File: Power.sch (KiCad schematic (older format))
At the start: 7 parts, among them J10 Conn_01x02_Female, U3 MCP73831T-2ACI_OT

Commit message: REAL COMMIT: Completed initial schematic. Added ADCs, Haptic FB circuits, test points, USB/Battery selection circuits.
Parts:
- removed D10: LED, symbol Device:LED
- added D3, D7: SS54, Diode_SMD:D_SMA_Handsoldering, symbol Device:D_Schottky
- added D4, D5, D6: 19-213/Y2C-CQ2R2L/3T, LEDs:LED_0603_HandSoldering, symbol Device:LED
- added Q1: DMG2305, Package_TO_SOT_SMD:SOT-23, symbol Transistor_FET:DMG2301L
- added R10, R11: 100k, Resistor_SMD:R_0603_1608Metric_Pad0.84x1.00mm_HandSolder, symbol Device:R
- added R8: 120, Resistor_SMD:R_0603_1608Metric_Pad0.84x1.00mm_HandSolder, symbol Device:R
- added R9: 300, Resistor_SMD:R_0603_1608Metric_Pad0.84x1.00mm_HandSolder, symbol Device:R
- C5: renamed from C11; footprint (none) -> Capacitors_SMD:C_0603_HandSoldering
- C6: renamed from C10; footprint (none) -> Capacitors_SMD:C_0603_HandSoldering
- J4: renamed from J10; footprint (none) -> Connector_JST:JST_PH_B2B-PH-SM4-TB_1x02_P2.00mm_Vertical
- R6: renamed from R10; value 2kR -> 2k; footprint Resistor_SMD:R_0402_1005Metric_Pad0.72x0.64mm_HandSolder -> Resistor_SMD:R_0402_1005Metric
- R7: renamed from R11; value 470R -> 270; footprint Resistor_SMD:R_1206_3216Metric_Pad1.30x1.75mm_HandSolder -> Resistor_SMD:R_0603_1608Metric_Pad0.84x1.00mm_HandSolder
- U1: renamed from U3; symbol dk_PMIC-Battery-Chargers:MCP73831T-2ACI_OT -> Glove-PCB-rescue:MCP73831T-2ACI_OT-dk_PMIC-Battery-Chargers
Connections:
- net labels added: +3.3V, +BATT, VBATT_OUT, VBUS, VDD
- net labels removed: 5V, VBatt
- wire segments 21 -> 51
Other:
- moved on the sheet: C6

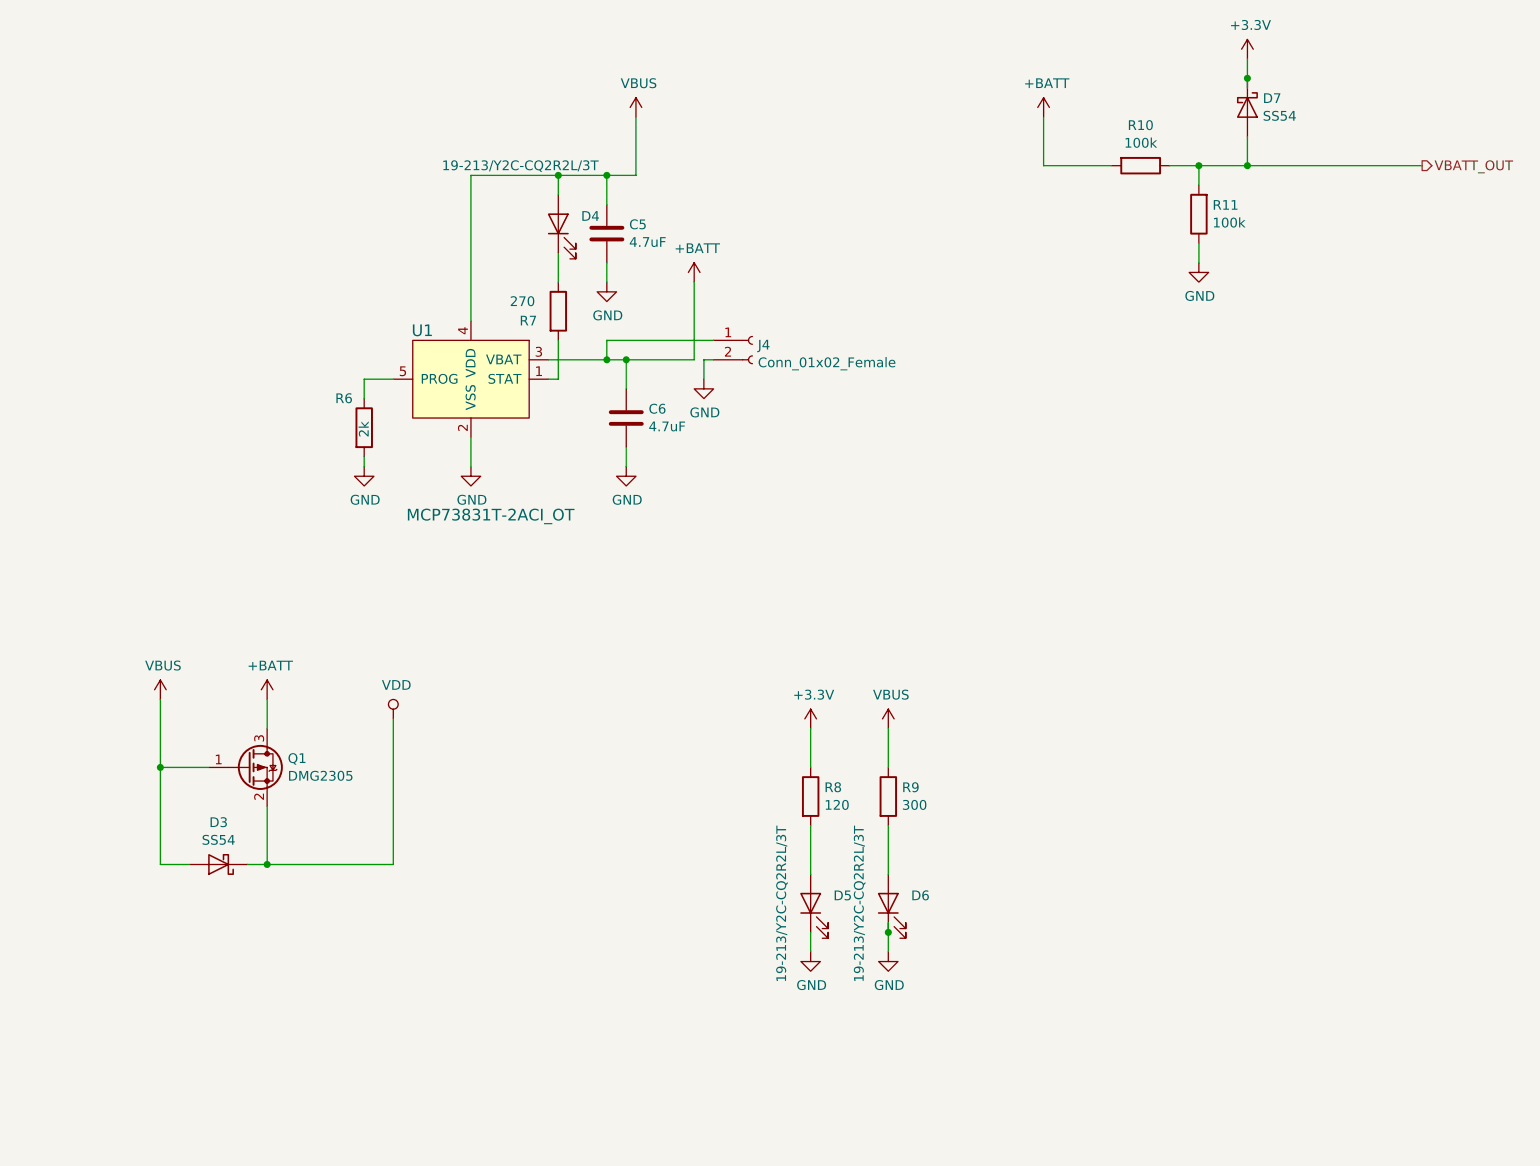
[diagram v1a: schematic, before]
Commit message: Added project and digikey footprints. Added mini-spox connectors.
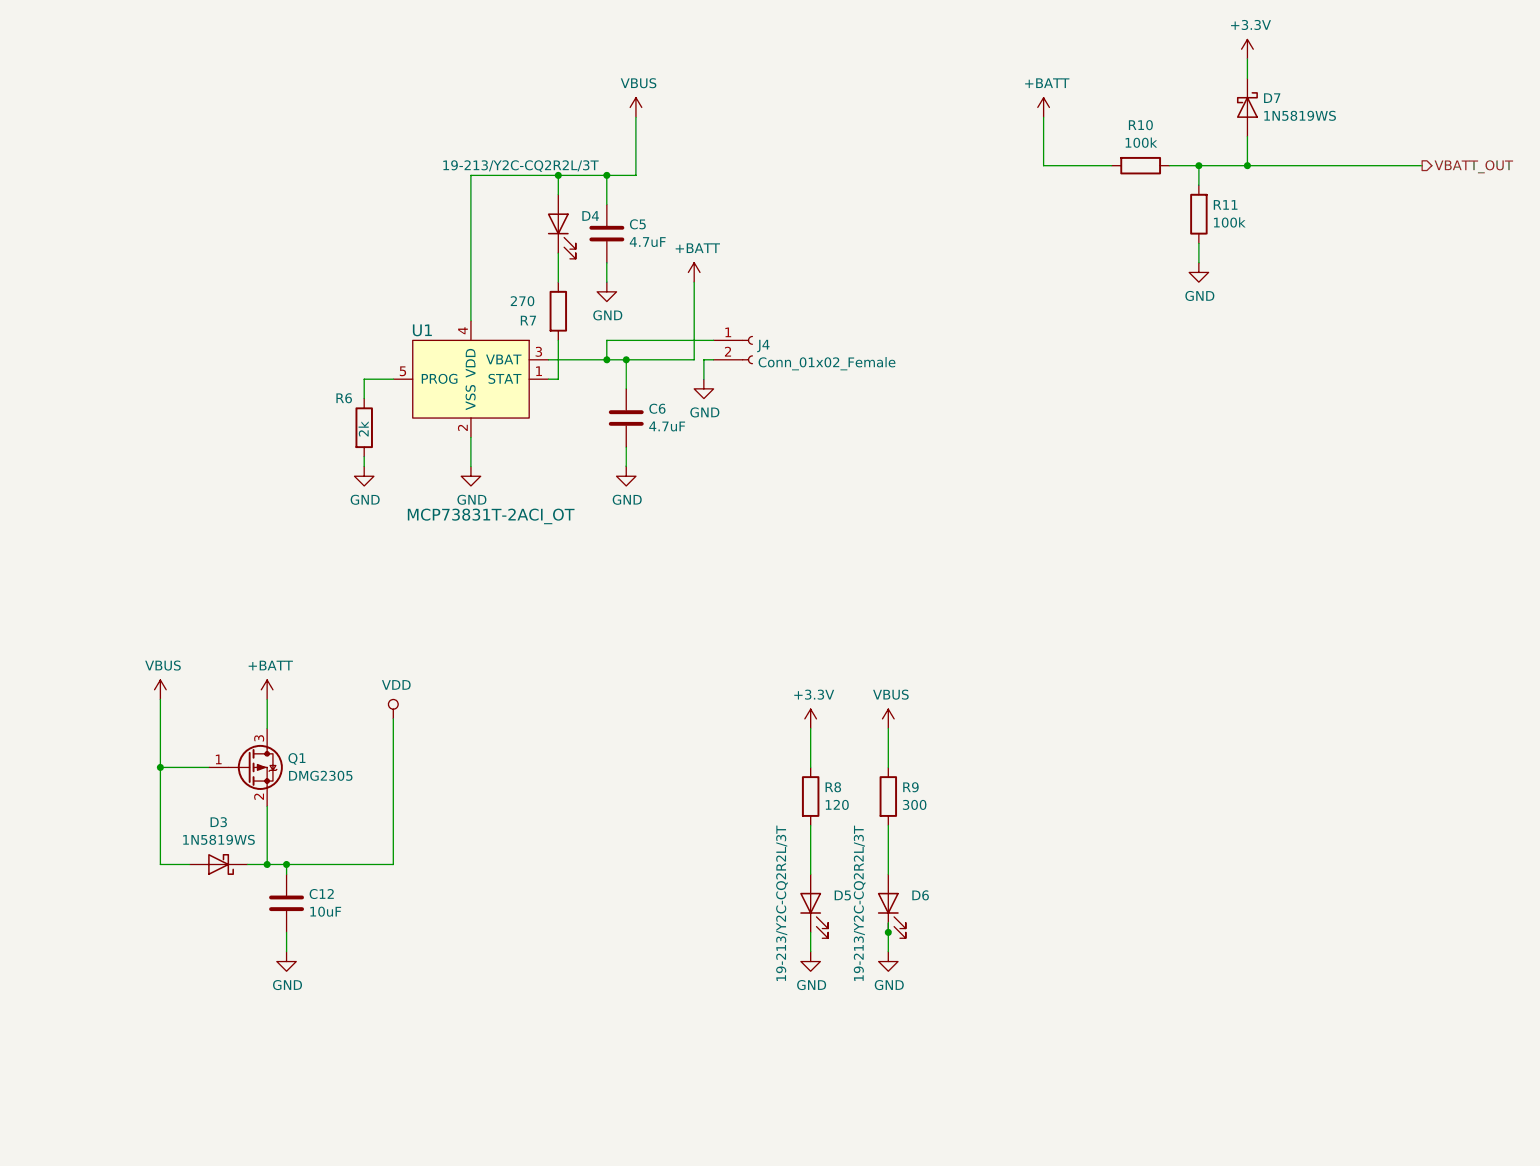
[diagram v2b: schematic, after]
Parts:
- added C12: 10uF, Capacitors_SMD:C_0603_HandSoldering, symbol Device:C
- D3, D7: value SS54 -> 1N5819WS; footprint Diode_SMD:D_SMA_Handsoldering -> Diode_SMD:D_SOD-323
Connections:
- wire segments 51 -> 53
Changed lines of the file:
@@
 P 2100 5450
 F 0 "D3" H 2100 5234 50  0000 C CNN
-F 1 "SS54" H 2100 5325 50  0000 C CNN
-F 2 "Diode_SMD:D_SMA_Handsoldering" H 2100 5450 50  0001 C CNN
+F 1 "1N5819WS" H 2100 5325 50  0000 C CNN
+F 2 "Diode_SMD:D_SOD-323" H 2100 5450 50  0001 C CNN
 F 3 "https://datasheet.lcsc.com/szlcsc/1903061001_MDD-Jiangsu-Yutai-Elec-SS54_C22452.pdf" H 2100 5450 50  0001 C CNN
 	1    2100 5450
@@
 Connection ~ 2350 5450
 Wire Wire Line
-	2350 5450 3000 5450
+	2350 5450 2450 5450
 $Comp
 L power:VDD #PWR019
@@
 P 7400 1550
 F 0 "D7" V 7354 1629 50  0000 L CNN
-F 1 "SS54" V 7445 1629 50  0000 L CNN
-F 2 "Diode_SMD:D_SMA_Handsoldering" H 7400 1550 50  0001 C CNN
+F 1 "1N5819WS" V 7445 1629 50  0000 L CNN
+F 2 "Diode_SMD:D_SOD-323" H 7400 1550 50  0001 C CNN
 F 3 "https://datasheet.lcsc.com/szlcsc/1903061001_MDD-Jiangsu-Yutai-Elec-SS54_C22452.pdf" H 7400 1550 50  0001 C CNN
 	1    7400 1550
@@
 $EndComp
 Wire Wire Line
-	7400 1300 7400 1400
-Wire Wire Line
 	6350 1850 6700 1850
-Connection ~ 7400 1400
-Wire Wire Line
-	7400 1400 7400 1450
 Wire Wire Line
 	7400 1700 7400 1850
@@
 	1    0    0    -1
 $EndComp
+Wire Wire Line
+	7400 1300 7400 1400
+$Comp
+L Device:C C?
+U 1 1 5FC6DCD7
+P 2450 5650
+AR Path="/5FC6DCD7" Ref="C?"  Part="1"
+AR Path="/5FB48E27/5FC6DCD7" Ref="C12"  Part="1"
+F 0 "C12" H 2565 5696 50  0000 L CNN
+F 1 "10uF" H 2565 5605 50  0000 L CNN
+F 2 "Capacitors_SMD:C_0603_HandSoldering" H 2488 5500 50  0001 C CNN
+F 3 "https://www.digikey.com/en/products/detail/samsung-electro-mechanics/CL10A106MQ8NNNC/3886777\\\\" H 2450 5650 50  0001 C CNN
+	1    2450 5650
+	1    0    0    -1
+$EndComp
+Wire Wire Line
+	2450 5500 2450 5450
+Connection ~ 2450 5450
+Wire Wire Line
+	2450 5450 3000 5450
+$Comp
+L power:GND #PWR071
+U 1 1 5FC6FC64
+P 2450 5900
+F 0 "#PWR071" H 2450 5650 50  0001 C CNN
+F 1 "GND" H 2455 5727 50  0000 C CNN
+F 2 "" H 2450 5900 50  0001 C CNN
+F 3 "" H 2450 5900 50  0001 C CNN
+	1    2450 5900
+	1    0    0    -1
+$EndComp
+Wire Wire Line
+	2450 5900 2450 5800
 $EndSCHEMATC

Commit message: Added high side R for sensors and buck-boost. Replaced 3.0V VRef with LDO. BOM rev 1. Finished layout. TODO: Silkscreen.
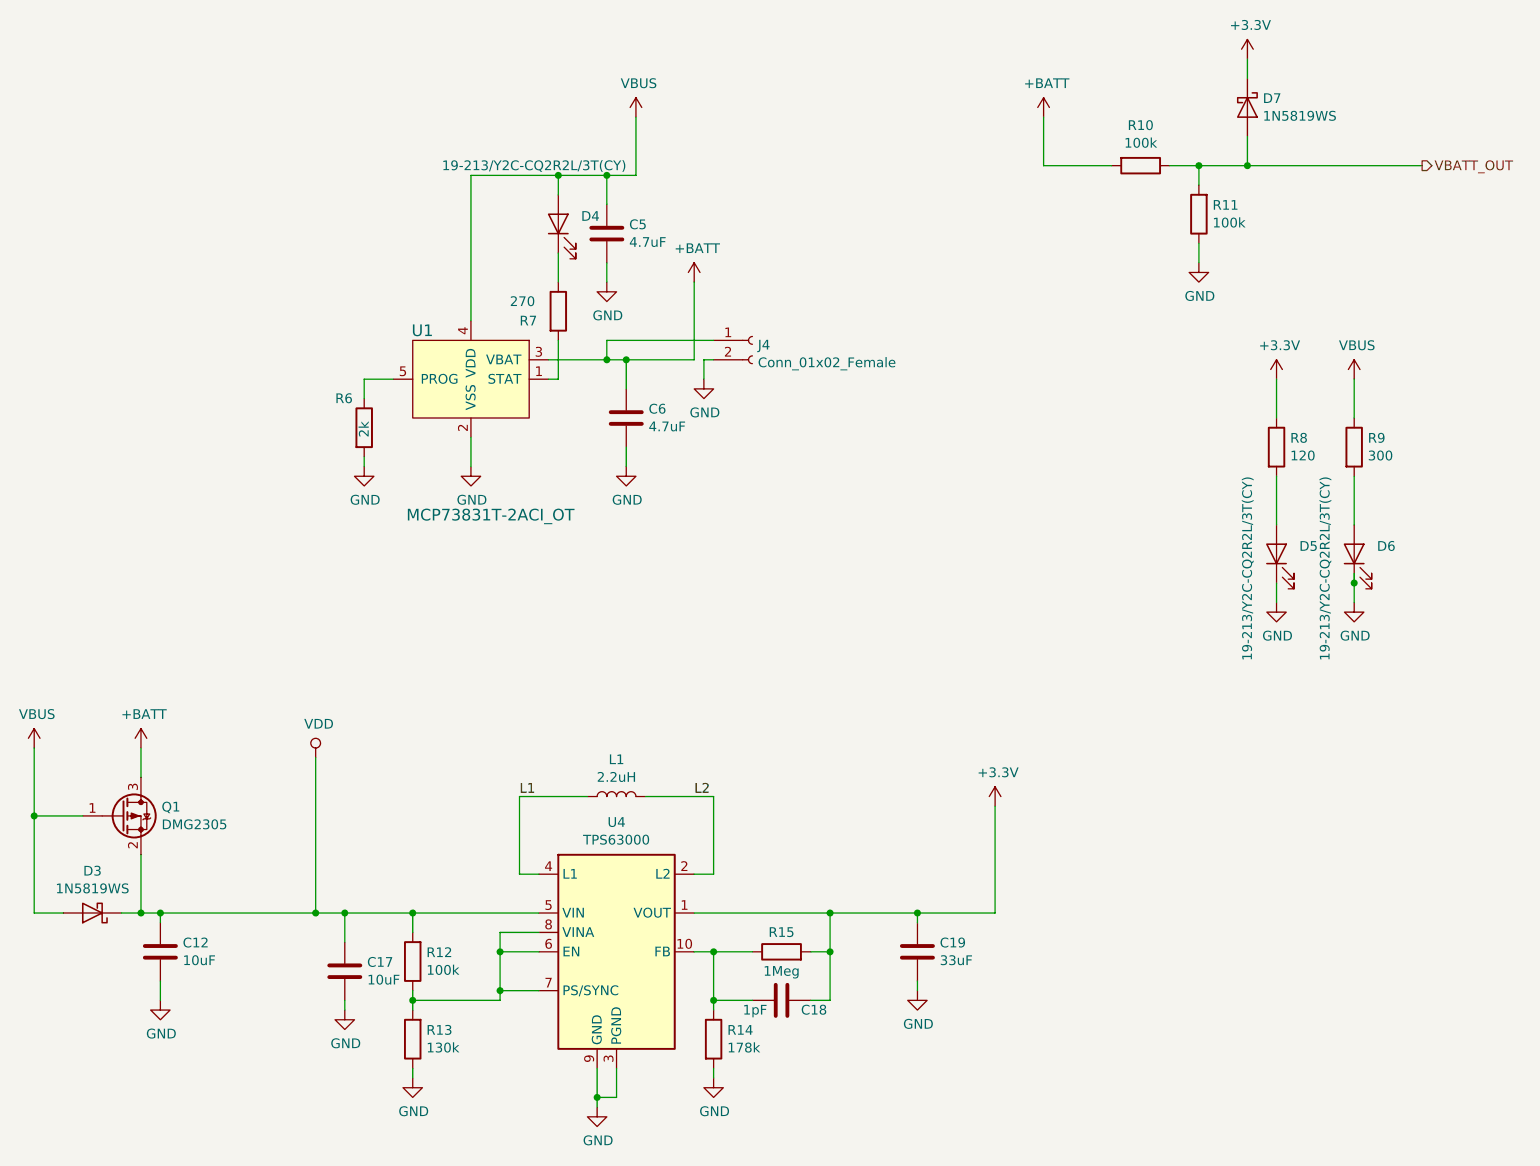
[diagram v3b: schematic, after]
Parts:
- added C17: 10uF, Capacitors_SMD:C_0603_HandSoldering, symbol Device:C
- added C18: 1pF, Capacitors_SMD:C_0603_HandSoldering, symbol Device:C
- added C19: 33uF, Capacitors_SMD:C_0805_HandSoldering, symbol Device:C
- added L1: 2.2uH, Inductors_SMD:L_0805_HandSoldering, symbol Device:L
- added R12: 100k, Resistors_SMD:R_0603_HandSoldering, symbol Device:R
- added R13: 130k, Resistors_SMD:R_0603_HandSoldering, symbol Device:R
- added R14: 178k, Resistors_SMD:R_0603_HandSoldering, symbol Device:R
- added R15: 1Meg, Resistors_SMD:R_0603_HandSoldering, symbol Device:R
- added U4: TPS63000, Package_SON:VSON-10-1EP_3x3mm_P0.5mm_EP1.65x2.4mm_ThermalVias, symbol Regulator_Switching:TPS63000
- C12: Description (none) -> MULTILAYER CERAMIC CAPACITORS MLCC - SMD/SMT 10UF 10V 0603 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; LCSC (none) -> C19702; MPN (none) -> CL10A106KP8NNNC; Manufacturer (none) -> Samsung Electro-Mechanics
- C5, C6: Description (none) -> MULTILAYER CERAMIC CAPACITORS MLCC - SMD/SMT 4.7UF 16V 0603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; LCSC (none) -> C19666; MPN (none) -> CL10A475KO8NNNC; Manufacturer (none) -> Samsung Electro-Mechanics
- D3, D7: Description (none) -> SCHOTTKY BARRIER DIODES (SBD) SOD-323 ROHS; LCSC (none) -> C191023; MPN (none) -> 1N5819WS; Manufacturer (none) -> Guangdong Hottech
- D4, D5, D6: value 19-213/Y2C-CQ2R2L/3T -> 19-213/Y2C-CQ2R2L/3T(CY); Description (none) -> LIGHT EMITTING DIODES (LED) YELLOW 585.5~591.5NM 90~180MCD@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; LCSC (none) -> C72038; MPN (none) -> 19-213/Y2C-CQ2R2L/3T(CY); Manufacturer (none) -> Everlight Elec
- J4: Description (none) -> -; LCSC (none) -> -; MPN (none) -> -; Manufacturer (none) -> -
- Q1: Description (none) -> MOSFET P TRENCH 20V 4.2A 900MV @ 250UA 52 M? @ 4.2A,4.5V SO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; LCSC (none) -> C144153; MPN (none) -> DMG2305UX-13; Manufacturer (none) -> DIODES INCORPORATED
- R10, R11: footprint Resistor_SMD:R_0603_1608Metric_Pad0.84x1.00mm_HandSolder -> Resistors_SMD:R_0603_HandSoldering; Description (none) -> CHIP RESISTOR - SURFACE MOUNT 100KOHMS ±1% 1/10W 0603 ROHS; LCSC (none) -> C25803; MPN (none) -> 0603WAF1003T5E; Manufacturer (none) -> Uniroyal Elec
- R6: Description (none) -> CHIP RESISTOR - SURFACE MOUNT 2KOHMS ±1% 1/16W 0402 ROHS; LCSC (none) -> C4109; MPN (none) -> 0402WGF2001TCE; Manufacturer (none) -> Uniroyal Elec
- R7: footprint Resistor_SMD:R_0603_1608Metric_Pad0.84x1.00mm_HandSolder -> Resistors_SMD:R_0603_HandSoldering; Description (none) -> CHIP RESISTOR - SURFACE MOUNT 270OHMS ±1% 1/10W 0603 ROHS; LCSC (none) -> C22966; MPN (none) -> 0603WAF2700T5E; Manufacturer (none) -> Uniroyal Elec
- R8: footprint Resistor_SMD:R_0603_1608Metric_Pad0.84x1.00mm_HandSolder -> Resistors_SMD:R_0603_HandSoldering; Description (none) -> CHIP RESISTOR - SURFACE MOUNT 120OHMS ±1% 1/10W 0603 ROHS; LCSC (none) -> C22787; MPN (none) -> 0603WAF1200T5E; Manufacturer (none) -> Uniroyal Elec
- R9: footprint Resistor_SMD:R_0603_1608Metric_Pad0.84x1.00mm_HandSolder -> Resistors_SMD:R_0603_HandSoldering; Description (none) -> CHIP RESISTOR - SURFACE MOUNT 300OHMS ±1% 1/10W 0603 ROHS; LCSC (none) -> C23025; MPN (none) -> 0603WAF3000T5E; Manufacturer (none) -> Uniroyal Elec
- U1: LCSC (none) -> C424093
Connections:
- net +3V3: now also C18.1, C19.1, R15.2, U4.1 (VOUT)
- net GND: now also C17.2, C19.2, R13.1, R14.2, U4.11 (PGND), U4.3 (PGND), U4.9 (GND)
- net VDD: now also C17.1, R12.2, U4.5 (VIN)
- new net: C18.2, R14.1, R15.1, U4.10 (FB)
- new net: R12.1, R13.2, U4.6 (EN), U4.7 (PS/SYNC), U4.8 (VINA)
- new net L1: L1.1, U4.4 (L1)
- new net L2: L1.2, U4.2 (L2)
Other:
- moved on the sheet: C12, D3, D5, D6, Q1, R8, R9
